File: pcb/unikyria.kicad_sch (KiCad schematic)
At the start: 60 parts, among them SW1 SW_PUSH, SW10 SW_PUSH, SW11 SW_PUSH, SW12 SW_PUSH, SW13 SW_PUSH, SW14 SW_PUSH, SW15 SW_PUSH, SW16 SW_PUSH, SW17 SW_PUSH, SW18 SW_PUSH, SW19 SW_PUSH, SW2 SW_PUSH, SW20 SW_PUSH, SW21 SW_PUSH, SW22 SW_PUSH, SW23 SW_PUSH, SW24 SW_PUSH, SW25 SW_Push, SW3 SW_PUSH, SW4 SW_PUSH, SW5 SW_PUSH, SW6 SW_PUSH, SW7 SW_PUSH, SW8 SW_PUSH, SW9 SW_PUSH, U1 kb2040, U2 MCP23S17_SO

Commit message: Work on PCBs.
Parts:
- removed JP1, JP2, JP3, JP4, JP5, JP6: SolderJumper_3_Open, Jumper:SolderJumper-3_P2.0mm_Open_TrianglePad1.0x1.5mm, symbol Jumper:SolderJumper_3_Open
- added D00B1, D01B1, D02B1, D03B1, D04B1, D05B1, D10B1, D11B1, D12B1, D13B1, D14B1, D15B1, D20B1, D21B1, D22B1, D23B1, D24B1, D25B1, D30B1, D31B1, D32B1, D33B1, D34B1, D35B1: 1N4148WT, Diode_SMD:D_SOD-523, symbol Diode:1N4148WT
- D05: renamed from D6; now left out of the parts list
- D30: renamed from D19; now left out of the parts list
- H_PAW_L1: renamed from H_PAW0; footprint Connector_PinHeader_1.00mm:PinHeader_1x08_P1.00mm_Horizontal -> Connector_PinHeader_2.54mm:PinHeader_1x08_P2.54mm_Horizontal
- SWL00: renamed from SW1; footprint footprints:CherryMX_Choc_Hotswap -> footprints:ChocV1_V2_Hotswap_18mm
- SWL01: renamed from SW2; footprint footprints:CherryMX_Choc_Hotswap -> footprints:ChocV1_V2_Hotswap_18mm
- SWL02: renamed from SW3; footprint footprints:CherryMX_Choc_Hotswap -> footprints:ChocV1_V2_Hotswap_18mm
- SWL03: renamed from SW4; footprint footprints:CherryMX_Choc_Hotswap -> footprints:ChocV1_V2_Hotswap_18mm
- SWL04: renamed from SW5; footprint footprints:CherryMX_Choc_Hotswap -> footprints:ChocV1_V2_Hotswap_18mm
- SWL05: renamed from SW6; footprint footprints:CherryMX_Choc_Hotswap -> footprints:ChocV1_V2_Hotswap_18mm; now left out of the parts list
- SWL10: renamed from SW7; footprint footprints:CherryMX_Choc_Hotswap -> footprints:ChocV1_V2_Hotswap_18mm
- SWL11: renamed from SW8; footprint footprints:CherryMX_Choc_Hotswap -> footprints:ChocV1_V2_Hotswap_18mm
- SWL12: renamed from SW9; footprint footprints:CherryMX_Choc_Hotswap -> footprints:ChocV1_V2_Hotswap_18mm
- SWL13: renamed from SW10; footprint footprints:CherryMX_Choc_Hotswap -> footprints:ChocV1_V2_Hotswap_18mm
- SWL14: renamed from SW11; footprint footprints:CherryMX_Choc_Hotswap -> footprints:ChocV1_V2_Hotswap_18mm
- SWL15: renamed from SW12; footprint footprints:CherryMX_Choc_Hotswap -> footprints:ChocV1_V2_Hotswap_18mm
- SWL20: renamed from SW13; footprint footprints:CherryMX_Choc_Hotswap -> footprints:ChocV1_V2_Hotswap_18mm
- SWL21: renamed from SW14; footprint footprints:CherryMX_Choc_Hotswap -> footprints:ChocV1_V2_Hotswap_18mm
- SWL22: renamed from SW15; footprint footprints:CherryMX_Choc_Hotswap -> footprints:ChocV1_V2_Hotswap_18mm
- SWL23: renamed from SW16; footprint footprints:CherryMX_Choc_Hotswap -> footprints:ChocV1_V2_Hotswap_18mm
- SWL24: renamed from SW17; footprint footprints:CherryMX_Choc_Hotswap -> footprints:ChocV1_V2_Hotswap_18mm
- SWL25: renamed from SW18; footprint footprints:CherryMX_Choc_Hotswap -> footprints:ChocV1_V2_Hotswap_18mm
- SWL30: renamed from SW19; footprint footprints:CherryMX_Choc_Hotswap -> footprints:ChocV1_V2_Hotswap_18mm; now left out of the parts list
- SWL31: renamed from SW20; footprint footprints:CherryMX_Choc_Hotswap -> footprints:ChocV1_V2_Hotswap_18mm
- SWL32: renamed from SW21; footprint footprints:CherryMX_Choc_Hotswap -> footprints:ChocV1_V2_Hotswap_18mm
- SWL33: renamed from SW22; footprint footprints:CherryMX_Choc_Hotswap -> footprints:ChocV1_V2_Hotswap_18mm
- SWL34: renamed from SW23; footprint footprints:CherryMX_Choc_Hotswap -> footprints:ChocV1_V2_Hotswap_18mm
- SWL35: renamed from SW24; footprint footprints:CherryMX_Choc_Hotswap -> footprints:ChocV1_V2_Hotswap_18mm
- renumbered D1 to D00, D2 to D01, D3 to D02, D4 to D03, D5 to D04, D7 to D10, D8 to D11, D9 to D12, D10 to D13, D11 to D14, D12 to D15, D13 to D20, D14 to D21, D15 to D22, D16 to D23, D17 to D24, D18 to D25, D20 to D31, D21 to D32, D22 to D33, D23 to D34, D24 to D35, JST_PH_INTC1 to JST_PH_INTC_L1, U2 to MCP_L1
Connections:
- net CS0: now also MCP_L1.11 (~{CS})
- net CS1: now also H_PAW_L1.5 (Pin_5)
- net INT0: now also MCP_L1.20 (INTA)
- net INT1: now also H_PAW_L1.6 (Pin_6)
- net R0: now also D00B1.1 (K), D01B1.1 (K), D02B1.1 (K), D03B1.1 (K), D04B1.1 (K), D05B1.1 (K)
- net R1: now also D10B1.1 (K), D11B1.1 (K), D12B1.1 (K), D13B1.1 (K), D14B1.1 (K), D15B1.1 (K)
- net R2: now also D20B1.1 (K), D21B1.1 (K), D22B1.1 (K), D23B1.1 (K), D24B1.1 (K), D25B1.1 (K)
- net R3: now also D30B1.1 (K), D31B1.1 (K), D32B1.1 (K), D33B1.1 (K), D34B1.1 (K), D35B1.1 (K)
- net RST0: now also MCP_L1.18 (~{RESET})
- net RST1: now also H_PAW_L1.8 (Pin_8)
- net at D21.2 (A), SWL21.1: now also D21B1.2 (A)
- net at D32.2 (A), SWL32.1: now also D32B1.2 (A)
- net at D23.2 (A), SWL23.1: now also D23B1.2 (A)
- net at D05.2 (A), SWL05.1: now also D05B1.2 (A)
- net at D30.2 (A), SWL30.1: now also D30B1.2 (A)
- net at D11.2 (A), SWL11.1: now also D11B1.2 (A)
- net at D33.2 (A), SWL33.1: now also D33B1.2 (A)
- net at D34.2 (A), SWL34.1: now also D34B1.2 (A)
- net at D04.2 (A), SWL04.1: now also D04B1.2 (A)
- net at D20.2 (A), SWL20.1: now also D20B1.2 (A)
- net at D12.2 (A), SWL12.1: now also D12B1.2 (A)
- net at D03.2 (A), SWL03.1: now also D03B1.2 (A)
- net at D01.2 (A), SWL01.1: now also D01B1.2 (A)
- net at D24.2 (A), SWL24.1: now also D24B1.2 (A)
- net at D31.2 (A), SWL31.1: now also D31B1.2 (A)
- net at D35.2 (A), SWL35.1: now also D35B1.2 (A)
- net at D13.2 (A), SWL13.1: now also D13B1.2 (A)
- net at D02.2 (A), SWL02.1: now also D02B1.2 (A)
- net at D15.2 (A), SWL15.1: now also D15B1.2 (A)
- net at D00.2 (A), SWL00.1: now also D00B1.2 (A)
- net at D10.2 (A), SWL10.1: now also D10B1.2 (A)
- net at D14.2 (A), SWL14.1: now also D14B1.2 (A)
- net at D25.2 (A), SWL25.1: now also D25B1.2 (A)
- net at D22.2 (A), SWL22.1: now also D22B1.2 (A)
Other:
- moved on the sheet: MCP_L1

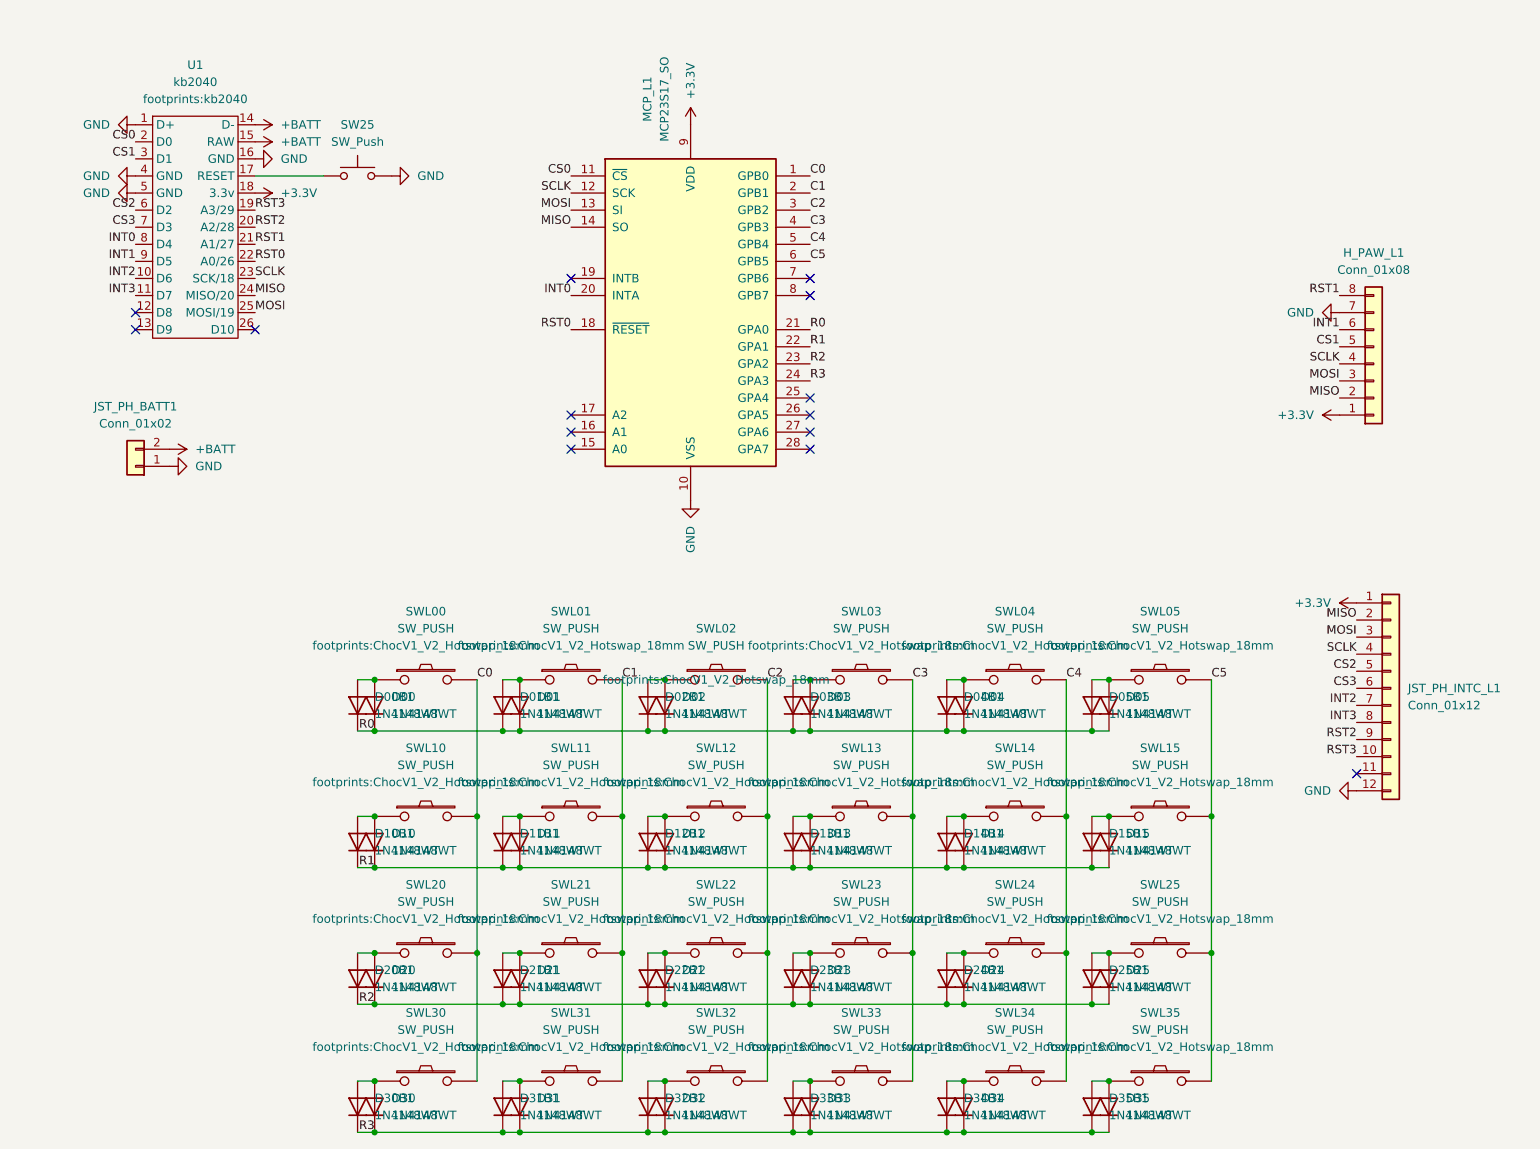
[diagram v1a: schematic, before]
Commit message: Replace KB2040 with XIAO nRF, work on PCB routing.
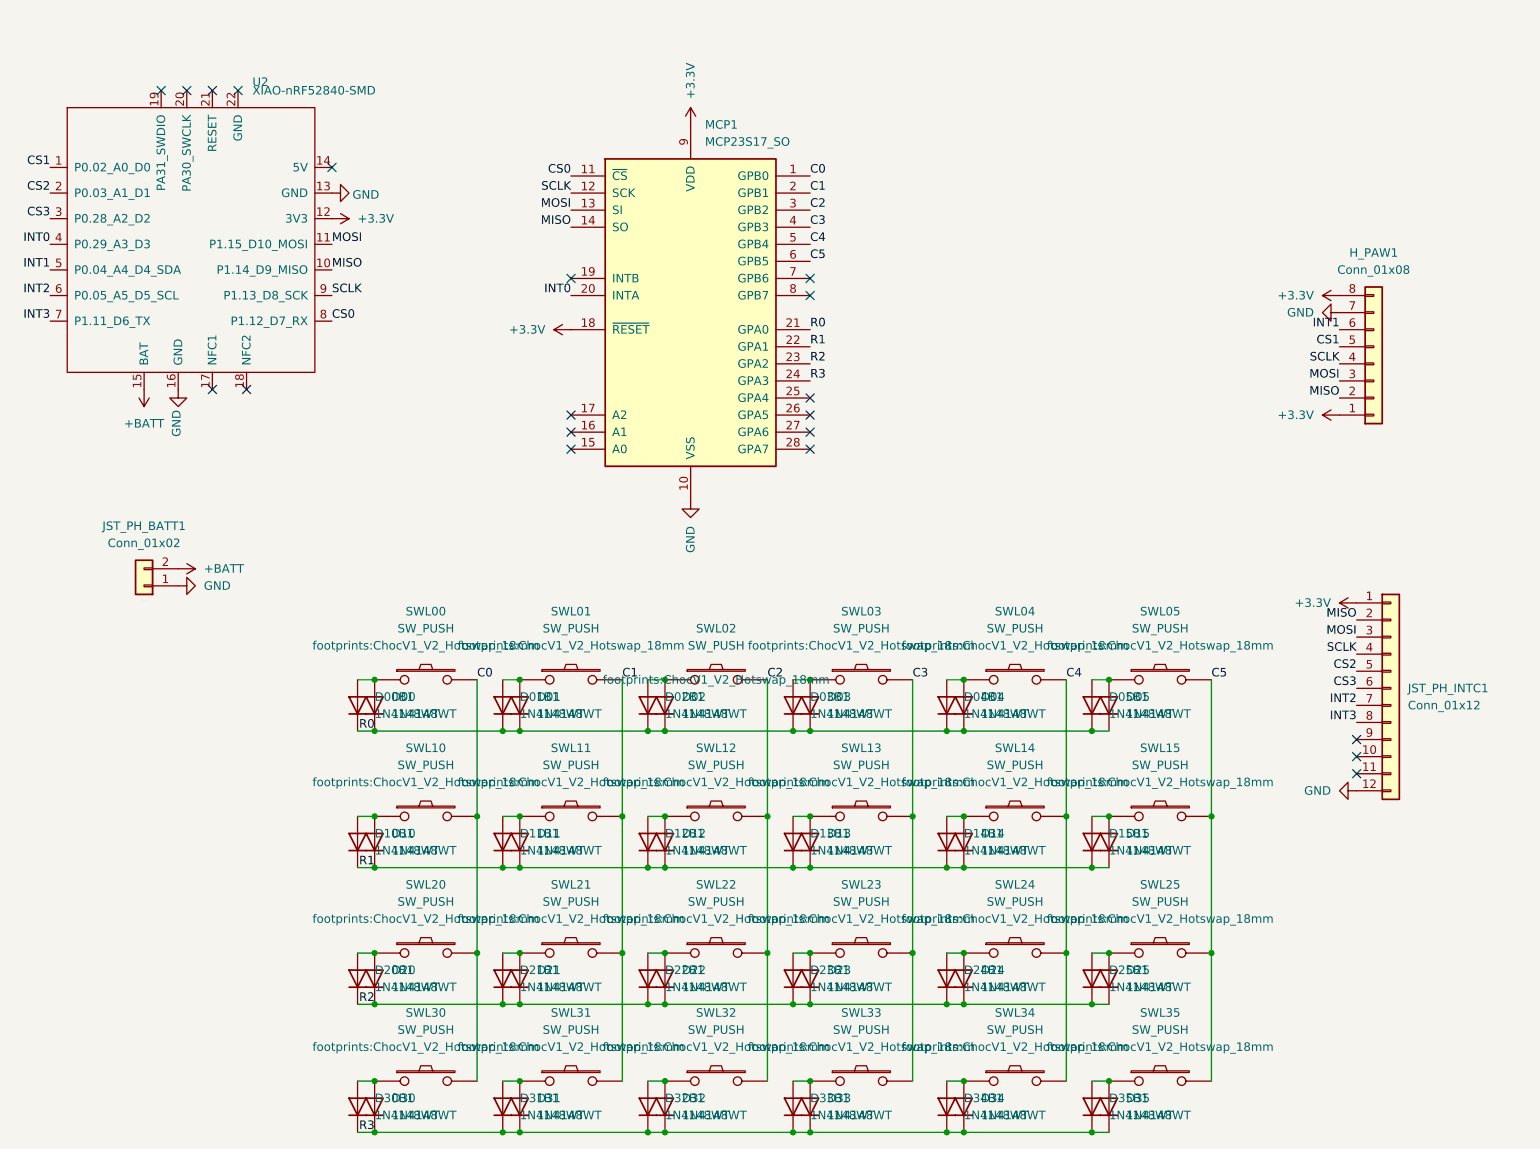
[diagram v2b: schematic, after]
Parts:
- removed SW25: SW_Push, Button_Switch_THT:SW_PUSH_6mm, symbol Switch:SW_Push
- removed U1: kb2040, footprints:kb2040, symbol kb2040:kb2040
- added U2: XIAO-nRF52840-SMD, footprints:XIAO-nRF52840-SMD, symbol Seeed_Studio_XIAO_Series:XIAO-nRF52840-SMD
- renumbered H_PAW_L1 to H_PAW1, JST_PH_INTC_L1 to JST_PH_INTC1, MCP_L1 to MCP1
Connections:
- net RST0 is gone; now on net +3.3V: MCP1.18 (~{RESET})
- net RST1 is gone; now on net +3.3V: H_PAW1.8 (Pin_8)
- net +3.3V: now also U2.12 (3V3)
- net +BATT: now also U2.15 (BAT)
- net CS0: now also U2.8 (P1.12_D7_RX)
- net CS1: now also U2.1 (P0.02_A0_D0)
- net CS2: now also U2.2 (P0.03_A1_D1)
- net CS3: now also U2.3 (P0.28_A2_D2)
- net GND: now also U2.13 (GND), U2.16 (GND)
- net INT0: now also U2.4 (P0.29_A3_D3)
- net INT1: now also U2.5 (P0.04_A4_D4_SDA)
- net INT2: now also U2.6 (P0.05_A5_D5_SCL)
- net INT3: now also U2.7 (P1.11_D6_TX)
- net MISO: now also U2.10 (P1.14_D9_MISO)
- net MOSI: now also U2.11 (P1.15_D10_MOSI)
- net SCLK: now also U2.9 (P1.13_D8_SCK)
- net RST2: no longer names the net of JST_PH_INTC1.9 (Pin_9)
- net RST3: no longer names the net of JST_PH_INTC1.10 (Pin_10)
- no-connect marks 14 -> 20
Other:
- moved on the sheet: JST_PH_BATT1
